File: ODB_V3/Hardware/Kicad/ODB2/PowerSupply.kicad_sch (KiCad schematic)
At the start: 53 parts, among them U13 L6981N33DR, U7 MPQ9843GLE-5-AEC1-Z

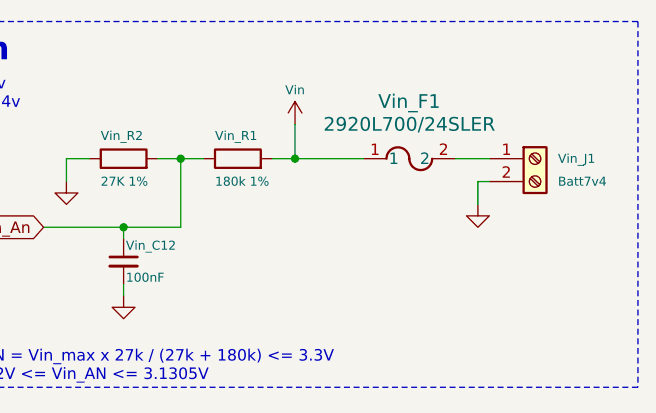
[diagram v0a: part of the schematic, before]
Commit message: fix: symbole errors and link missing footprints
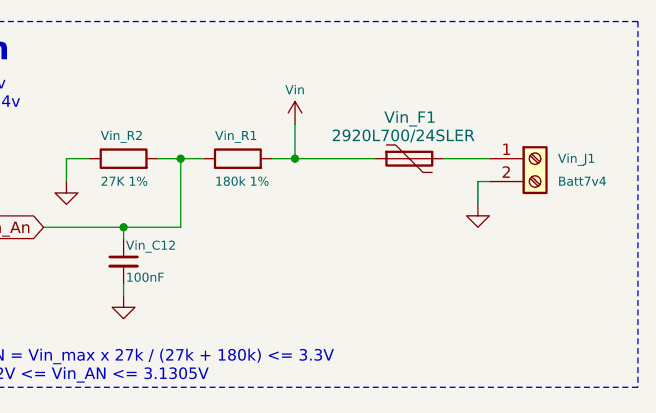
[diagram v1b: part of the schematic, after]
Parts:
- removed Vin_F1: 2920L700/24SLER, Fuse:Fuse_2920_7451Metric, symbol RGEF1400:RGEF1400
- added Vin_F1: 2920L700/24SLER, Fuse:Fuse_2920_7451Metric, symbol Device:Polyfuse
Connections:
- net Vin: now also Vin_F1.1
- net at Vin_J1.1 (Pin_1): now also Vin_F1.2
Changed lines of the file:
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@@
 	(wire
 		(pts
+			(xy 261.62 27.94) (xy 266.7 27.94)
+		)
+		(stroke
+			(width 0)
+			(type default)
+		)
+	)
+	(wire
+		(pts
 			(xy 68.58 35.56) (xy 68.58 34.29)
 		)
@@
 	(wire
 		(pts
-			(xy 245.11 27.94) (xy 252.73 27.94)
+			(xy 245.11 27.94) (xy 254 27.94)
 		)
 		(stroke
@@
 	(wire
 		(pts
-			(xy 262.89 27.94) (xy 266.7 27.94)
-		)
-		(stroke
-			(width 0)
-			(type default)
-		)
-	)
-	(wire
-		(pts
 			(xy 30.48 113.03) (xy 30.48 114.3)
 		)
@@
 	)
 	(symbol
-		(lib_id "RGEF1400:RGEF1400")
-		(at 252.73 27.94 0)
-		(unit 1)
-		(exclude_from_sim no)
-		(in_bom yes)
-		(on_board yes)
-		(dnp no)
-		(fields_autoplaced yes)
-		(property "Reference" "Vin_F1"
-			(at 257.81 21.59 0)
-			(effects
-				(font
-					(size 1.524 1.524)
-				)
-			)
-		)
-		(property "Value" "2920L700/24SLER"
-			(at 257.81 24.13 0)
-			(effects
-				(font
-					(size 1.524 1.524)
-				)
-			)
-		)
-		(property "Footprint" "Fuse:Fuse_2920_7451Metric"
-			(at 252.73 27.94 0)
-			(effects
-				(font
-					(size 1.27 1.27)
-					(italic yes)
-				)
-				(hide yes)
-			)
-		)
-		(property "Datasheet" "2920L700/12MR"
-			(at 252.73 27.94 0)
-			(effects
-				(font
-					(size 1.27 1.27)
-					(italic yes)
-				)
-				(hide yes)
-			)
-		)
-		(property "Description" ""
-			(at 252.73 27.94 0)
-			(effects
-				(font
-					(size 1.27 1.27)
-				)
-				(hide yes)
-			)
-		)
-		(pin "1"
-		)
-		(pin "2"
-		)
-		(instances
-			(project "ODB2"
-				(path "/4b06c5d1-aa8b-48ed-8972-b43a60cfab78/a0dfa29e-ccca-4096-8481-c7e33c67aac5"
-					(reference "Vin_F1")
-					(unit 1)
-				)
-			)
-		)
-	)
-	(symbol
 		(lib_id "power:GND")
 		(at 87.63 158.75 0)
@@
 					(unit 1)
 				)
+			)
+		)
+	)
+	(symbol
+		(lib_id "Device:Polyfuse")
+		(at 257.81 27.94 90)
+		(mirror x)
+		(unit 1)
+		(exclude_from_sim no)
+		(in_bom yes)
+		(on_board yes)
+		(dnp no)
+		(property "Reference" "Vin_F1"
+			(at 255.016 23.368 90)
+			(effects
+				(font
+					(size 1.27 1.27)
+				)
+				(justify right)
+			)
+		)
+		(property "Value" "2920L700/24SLER"
+			(at 249.174 25.4 90)
+			(effects
+				(font
+					(size 1.27 1.27)
+				)
+				(justify right)
+			)
+		)
+		(property "Footprint" "Fuse:Fuse_2920_7451Metric"
+			(at 262.89 29.21 0)
+			(effects
+				(font
+					(size 1.27 1.27)
+				)
+				(justify left)
+				(hide yes)
+			)
+		)
+		(property "Datasheet" "2920L700/24SLER"
+			(at 257.81 27.94 0)
+			(effects
+				(font
+					(size 1.27 1.27)
+				)
+				(hide yes)
+			)
+		)
+		(property "Description" "Resettable fuse"
+			(at 257.81 27.94 0)
+			(effects
+				(font
+					(size 1.27 1.27)
+				)
+				(hide yes)
+			)
+		)
+		(pin "2"
+		)
+		(pin "1"
+		)
+		(instances
+			(project ""
+				(path "/4b06c5d1-aa8b-48ed-8972-b43a60cfab78/a0dfa29e-ccca-4096-8481-c7e33c67aac5"
+					(reference "Vin_F1")
+					(unit 1)
+				)

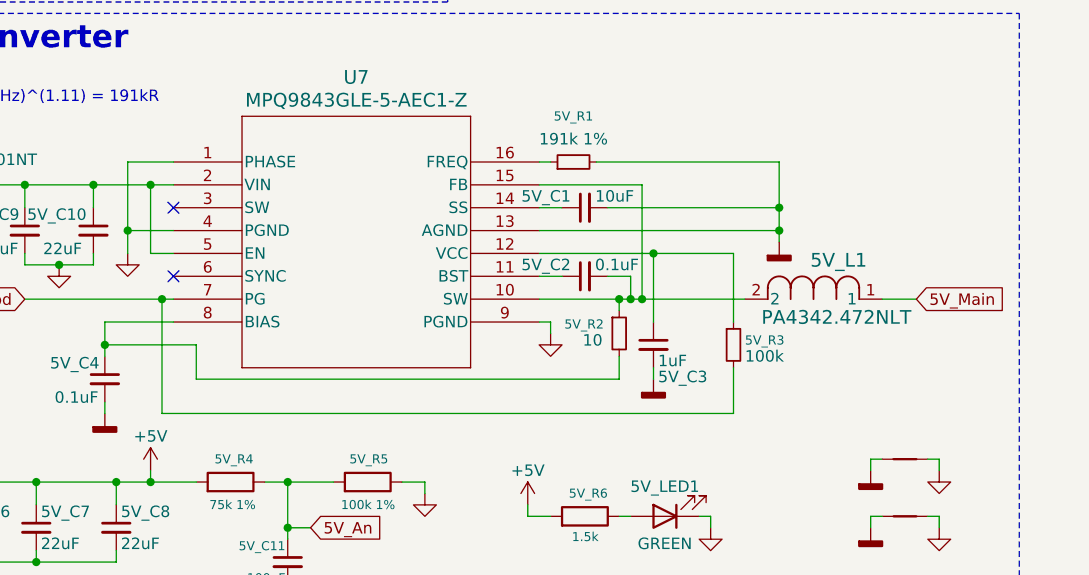
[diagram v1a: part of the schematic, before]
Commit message: fix: bias + FB feedback after inductance in buck converter 5V
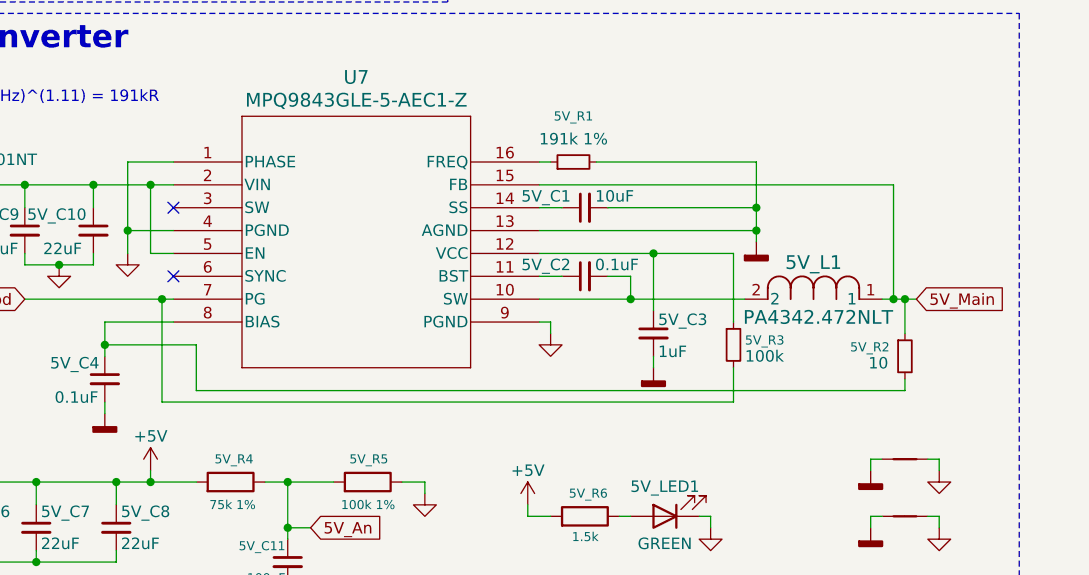
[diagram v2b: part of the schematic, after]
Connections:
- net +5V: now also 5V_R2.1, U7.15 (FB)
- net at 5V_C2.2, 5V_L1.2, U7.10 (SW): no longer 5V_R2.1, U7.15 (FB)
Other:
- moved on the sheet: 5V_C3, 5V_R2
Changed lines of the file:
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@@
 	)
 	(junction
-		(at 130.81 73.66)
+		(at 128.27 73.66)
 		(diameter 0)
 		(color 0 0 0 0)
@@
 	)
 	(junction
+		(at 143.51 83.82)
+		(diameter 0)
+		(color 0 0 0 0)
+	)
+	(junction
 		(at 46.99 71.12)
 		(diameter 0)
@@
 	)
 	(junction
-		(at 130.81 76.2)
+		(at 128.27 76.2)
 		(diameter 0)
 		(color 0 0 0 0)
@@
 	)
 	(junction
-		(at 115.57 83.82)
-		(diameter 0)
-		(color 0 0 0 0)
-	)
-	(junction
 		(at 83.82 181.61)
 		(diameter 0)
@@
 	)
 	(junction
-		(at 113.03 83.82)
-		(diameter 0)
-		(color 0 0 0 0)
-	)
-	(junction
 		(at 63.5 41.91)
 		(diameter 0)
@@
 		(color 0 0 0 0)
 	)
+	(junction
+		(at 144.78 83.82)
+		(diameter 0)
+		(color 0 0 0 0)
+	)
 	(no_connect
 		(at 63.5 73.66)
@@
 	(wire
 		(pts
-			(xy 110.49 68.58) (xy 130.81 68.58)
+			(xy 110.49 68.58) (xy 128.27 68.58)
+		)
+		(stroke
+			(width 0)
+			(type default)
+		)
+	)
+	(wire
+		(pts
+			(xy 143.51 83.82) (xy 144.78 83.82)
 		)
 		(stroke
@@
 	(wire
 		(pts
-			(xy 130.81 68.58) (xy 130.81 73.66)
+			(xy 144.78 83.82) (xy 144.78 87.63)
 		)
 		(stroke
@@
 	(wire
 		(pts
-			(xy 62.23 96.52) (xy 62.23 83.82)
+			(xy 128.27 68.58) (xy 128.27 73.66)
+		)
+		(stroke
+			(width 0)
+			(type default)
+		)
+	)
+	(wire
+		(pts
+			(xy 62.23 95.25) (xy 62.23 83.82)
 		)
 		(stroke
@@
 	(wire
 		(pts
-			(xy 66.04 92.71) (xy 66.04 88.9)
+			(xy 66.04 93.98) (xy 66.04 88.9)
 		)
 		(stroke
@@
 	(wire
 		(pts
-			(xy 142.24 83.82) (xy 146.05 83.82)
+			(xy 142.24 83.82) (xy 143.51 83.82)
 		)
 		(stroke
@@
 	(wire
 		(pts
-			(xy 113.03 90.17) (xy 113.03 92.71)
-		)
-		(stroke
-			(width 0)
-			(type default)
-		)
-	)
-	(wire
-		(pts
 			(xy 57.15 185.42) (xy 48.26 185.42)
 		)
@@
 	(wire
 		(pts
-			(xy 130.81 73.66) (xy 130.81 76.2)
+			(xy 128.27 73.66) (xy 128.27 76.2)
 		)
 		(stroke
@@
 	(wire
 		(pts
-			(xy 113.03 83.82) (xy 114.3 83.82)
-		)
-		(stroke
-			(width 0)
-			(type default)
-		)
-	)
-	(wire
-		(pts
 			(xy 91.44 105.41) (xy 91.44 104.14)
 		)
@@
 	(wire
 		(pts
-			(xy 104.14 83.82) (xy 113.03 83.82)
+			(xy 104.14 83.82) (xy 114.3 83.82)
 		)
 		(stroke
@@
 	(wire
 		(pts
-			(xy 113.03 83.82) (xy 113.03 85.09)
-		)
-		(stroke
-			(width 0)
-			(type default)
-		)
-	)
-	(wire
-		(pts
 			(xy 30.48 41.91) (xy 39.37 41.91)
 		)
@@
 	(wire
 		(pts
-			(xy 116.84 91.44) (xy 116.84 92.71)
+			(xy 48.26 113.03) (xy 39.37 113.03)
 		)
 		(stroke
@@
 	(wire
 		(pts
-			(xy 48.26 113.03) (xy 39.37 113.03)
+			(xy 144.78 83.82) (xy 146.05 83.82)
 		)
 		(stroke
@@
 	(wire
 		(pts
-			(xy 62.23 96.52) (xy 125.73 96.52)
+			(xy 62.23 95.25) (xy 125.73 95.25)
 		)
 		(stroke
@@
 	(wire
 		(pts
-			(xy 114.3 83.82) (xy 115.57 83.82)
+			(xy 114.3 83.82) (xy 127 83.82)
 		)
 		(stroke
@@
 	(wire
 		(pts
-			(xy 130.81 77.47) (xy 130.81 76.2)
+			(xy 128.27 77.47) (xy 128.27 76.2)
 		)
 		(stroke
@@
 	(wire
 		(pts
-			(xy 104.14 76.2) (xy 130.81 76.2)
+			(xy 104.14 76.2) (xy 128.27 76.2)
 		)
 		(stroke
@@
 	(wire
 		(pts
-			(xy 113.03 92.71) (xy 66.04 92.71)
+			(xy 66.04 93.98) (xy 144.78 93.98)
 		)
 		(stroke
@@
 	(wire
 		(pts
-			(xy 116.84 86.36) (xy 116.84 78.74)
+			(xy 116.84 85.09) (xy 116.84 78.74)
 		)
 		(stroke
@@
 	(wire
 		(pts
-			(xy 115.57 83.82) (xy 127 83.82)
+			(xy 116.84 91.44) (xy 116.84 90.17)
 		)
 		(stroke
@@
 	(wire
 		(pts
-			(xy 104.14 71.12) (xy 115.57 71.12)
+			(xy 104.14 71.12) (xy 143.51 71.12)
 		)
 		(stroke
@@
 	(wire
 		(pts
-			(xy 125.73 91.44) (xy 125.73 96.52)
+			(xy 125.73 91.44) (xy 125.73 95.25)
 		)
 		(stroke
@@
 	(wire
 		(pts
-			(xy 111.76 73.66) (xy 130.81 73.66)
+			(xy 111.76 73.66) (xy 128.27 73.66)
 		)
 		(stroke
@@
 	(wire
 		(pts
-			(xy 115.57 71.12) (xy 115.57 83.82)
+			(xy 143.51 71.12) (xy 143.51 83.82)
 		)
 		(stroke
@@
 	(wire
 		(pts
+			(xy 144.78 93.98) (xy 144.78 92.71)
+		)
+		(stroke
+			(width 0)
+			(type default)
+		)
+	)
+	(wire
+		(pts
 			(xy 217.17 35.56) (xy 226.06 35.56)
 		)
@@
 	(symbol
 		(lib_id "power:GNDD")
-		(at 130.81 77.47 0)
+		(at 128.27 77.47 0)
 		(unit 1)
 		(exclude_from_sim no)
@@
 		(fields_autoplaced yes)
 		(property "Reference" "#PWR06"
-			(at 130.81 83.82 0)
+			(at 128.27 83.82 0)
 			(effects
 				(font
@@
 		)
 		(property "Value" "AGND5V"
-			(at 130.81 81.28 0)
+			(at 128.27 81.28 0)
 			(effects
 				(font
@@
 		)
 		(property "Footprint" ""
-			(at 130.81 77.47 0)
+			(at 128.27 77.47 0)
 			(effects
 				(font
@@
 		)
 		(property "Datasheet" ""
-			(at 130.81 77.47 0)
+			(at 128.27 77.47 0)
 			(effects
 				(font
@@
 		)
 		(property "Description" "Power symbol creates a global label with name \"GNDD\" , digital ground"
-			(at 130.81 77.47 0)
+			(at 128.27 77.47 0)
 			(effects
 				(font
@@
 		(dnp no)
 		(property "Reference" "5V_L1"
-			(at 137.414 79.502 0)
+			(at 134.62 79.756 0)
 			(effects
 				(font
@@
 		)
 		(property "Value" "PA4342.472NLT"
-			(at 137.16 85.852 0)
+			(at 135.128 85.852 0)
 			(effects
 				(font
@@
 	(symbol
 		(lib_id "power:GNDD")
-		(at 116.84 92.71 0)
+		(at 116.84 91.44 0)
 		(unit 1)
 		(exclude_from_sim no)
@@
 		(fields_autoplaced yes)
 		(property "Reference" "#PWR02"
-			(at 116.84 99.06 0)
+			(at 116.84 97.79 0)
 			(effects
 				(font
@@
 		)
 		(property "Value" "AGND5V"
-			(at 116.84 96.52 0)
+			(at 116.84 95.25 0)
 			(effects
 				(font
@@
 		)
 		(property "Footprint" ""
-			(at 116.84 92.71 0)
+			(at 116.84 91.44 0)
 			(effects
 				(font
@@
 		)
 		(property "Datasheet" ""
-			(at 116.84 92.71 0)
+			(at 116.84 91.44 0)
 			(effects
 				(font
@@
 		)
 		(property "Description" "Power symbol creates a global label with name \"GNDD\" , digital ground"
-			(at 116.84 92.71 0)
+			(at 116.84 91.44 0)
 			(effects
 				(font
@@
 	(symbol
 		(lib_id "Device:R_Small")
-		(at 113.03 87.63 0)
+		(at 144.78 90.17 0)
 		(unit 1)
 		(exclude_from_sim no)
@@
 		(dnp no)
 		(property "Reference" "5V_R2"
-			(at 106.934 86.614 0)
+			(at 138.684 89.154 0)
 			(effects
 				(font
@@
 		)
 		(property "Value" "10"
-			(at 108.966 88.392 0)
+			(at 140.716 90.932 0)
 			(effects
 				(font
@@
 		)
 		(property "Footprint" "Resistor_SMD:R_0603_1608Metric"
-			(at 113.03 87.63 0)
+			(at 144.78 90.17 0)
 			(effects
 				(font
@@
 		)
 		(property "Datasheet" "~"
-			(at 113.03 87.63 0)
+			(at 144.78 90.17 0)
 			(effects
 				(font
@@
 		)
 		(property "Description" "Resistor, small symbol"
-			(at 113.03 87.63 0)
+			(at 144.78 90.17 0)
 			(effects
 				(font
@@
 		)
 		(instances
-			(project ""
+			(project "ODB2"
 				(path "/4b06c5d1-aa8b-48ed-8972-b43a60cfab78/a0dfa29e-ccca-4096-8481-c7e33c67aac5"
 					(reference "5V_R2")
@@
 	(symbol
 		(lib_id "Device:C_Small")
-		(at 116.84 88.9 0)
+		(at 116.84 87.63 0)
 		(unit 1)
 		(exclude_from_sim no)
@@
 		(dnp no)
 		(property "Reference" "5V_C3"
-			(at 117.348 92.456 0)
+			(at 117.348 86.106 0)
 			(effects
 				(font
@@
 		)
 		(property "Value" "1uF"
-			(at 117.348 90.678 0)
+			(at 117.348 89.662 0)
 			(effects
 				(font
@@
 		)
 		(property "Footprint" "Capacitor_SMD:C_0603_1608Metric"
-			(at 116.84 88.9 0)
+			(at 116.84 87.63 0)
 			(effects
 				(font
@@
 		)
 		(property "Datasheet" "~"
-			(at 116.84 88.9 0)
+			(at 116.84 87.63 0)
 			(effects
 				(font
@@
 		)
 		(property "Description" "Unpolarized capacitor, small symbol"
-			(at 116.84 88.9 0)
+			(at 116.84 87.63 0)
 			(effects
 				(font

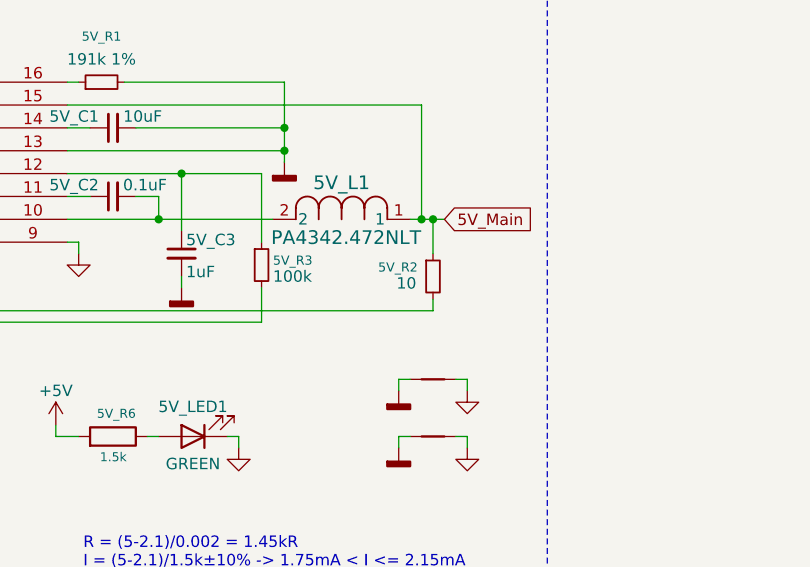
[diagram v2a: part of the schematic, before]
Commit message: fix label 5V_R2
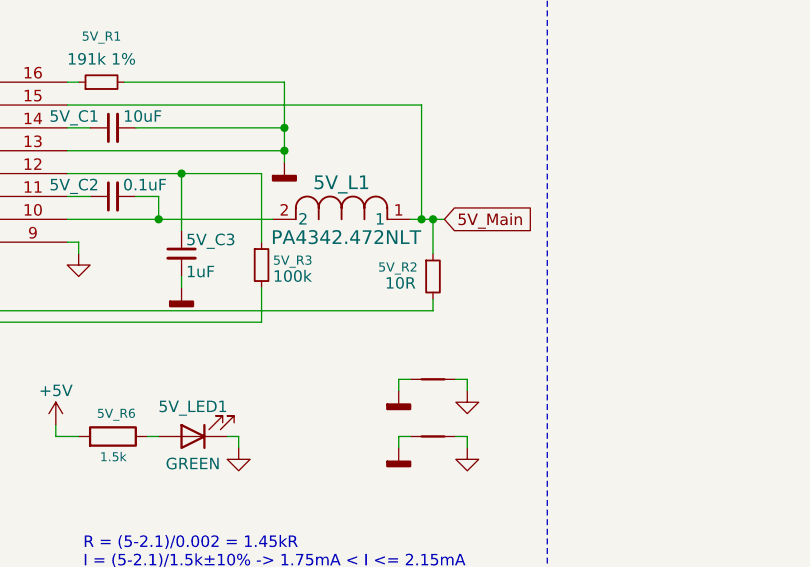
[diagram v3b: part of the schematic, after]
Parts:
- 5V_R2: value 10 -> 10R
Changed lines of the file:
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@@
 			)
 		)
-		(property "Value" "10"
-			(at 140.716 90.932 0)
+		(property "Value" "10R"
+			(at 139.446 90.932 0)
 			(effects
 				(font

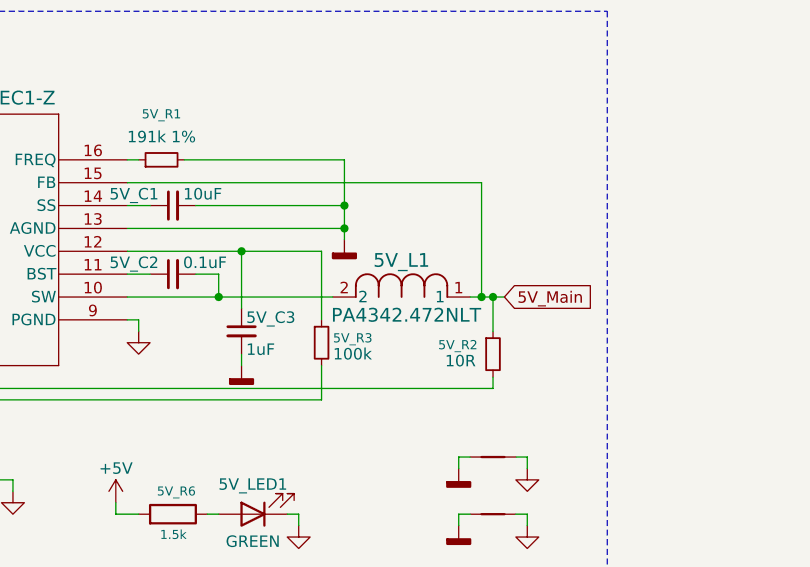
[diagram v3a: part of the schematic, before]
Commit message: fix: some footprints/symboles link + add criticalLed pin
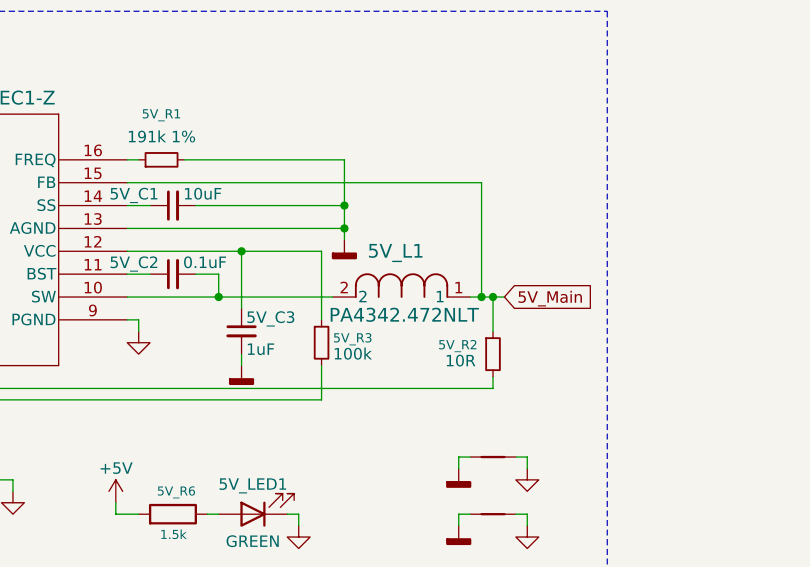
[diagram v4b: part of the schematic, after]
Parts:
- 5V_L1: footprint IND_PA4342_PUL -> ODB:IND_PA4342_PUL
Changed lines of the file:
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@@
+	)
+	(symbol
+		(lib_name "PA4342.472NLT_1")
+		(lib_id "ODB2:PA4342.472NLT")
+		(at 127 83.82 0)
+		(unit 1)
+		(exclude_from_sim no)
+		(in_bom yes)
+		(on_board yes)
+		(dnp no)
+		(property "Reference" "5V_L1"
+			(at 133.985 78.74 0)
+			(effects
+				(font
+					(size 1.524 1.524)
+				)
+			)
+		)
+		(property "Value" "PA4342.472NLT"
+			(at 134.874 85.852 0)
+			(effects
+				(font
+					(size 1.524 1.524)
+				)
+			)
+		)
+		(property "Footprint" "ODB:IND_PA4342_PUL"
+			(at 127 83.82 0)
+			(effects
+				(font
+					(size 1.27 1.27)
+					(italic yes)
+				)
+				(hide yes)
+			)
+		)
+		(property "Datasheet" "PA4342.472NLT"
+			(at 127 83.82 0)
+			(effects
+				(font
+					(size 1.27 1.27)
+					(italic yes)
+				)
+				(hide yes)
+			)
+		)
+		(property "Description" ""
+			(at 127 83.82 0)
+			(effects
+				(font
+					(size 1.27 1.27)
+				)
+				(hide yes)
+			)
+		)
+		(pin "2"
+		)
+		(pin "1"
+		)
+		(instances
+			(project ""
+				(path "/4b06c5d1-aa8b-48ed-8972-b43a60cfab78/a0dfa29e-ccca-4096-8481-c7e33c67aac5"
+					(reference "5V_L1")
+					(unit 1)
+				)
+			)
+		)
 	)
 	(symbol
@@
 					(unit 1)
 				)
-			)
-		)
-	)
-	(symbol
-		(lib_id "ODB2:PA4342.472NLT")
-		(at 127 83.82 0)
-		(unit 1)
-		(exclude_from_sim no)
-		(in_bom yes)
-		(on_board yes)
-		(dnp no)
-		(property "Reference" "5V_L1"
-			(at 134.62 79.756 0)
-			(effects
-				(font
-					(size 1.524 1.524)
-				)
-			)
-		)
-		(property "Value" "PA4342.472NLT"
-			(at 135.128 85.852 0)
-			(effects
-				(font
-					(size 1.524 1.524)
-				)
-			)
-		)
-		(property "Footprint" "IND_PA4342_PUL"
-			(at 127 83.82 0)
-			(effects
-				(font
-					(size 1.27 1.27)
-					(italic yes)
-				)
-				(hide yes)
-			)
-		)
-		(property "Datasheet" "PA4342.472NLT"
-			(at 127 83.82 0)
-			(effects
-				(font
-					(size 1.27 1.27)
-					(italic yes)
-				)
-				(hide yes)
-			)
-		)
-		(property "Description" ""
-			(at 127 83.82 0)
-			(effects
-				(font
-					(size 1.27 1.27)
-				)
-				(hide yes)
-			)
-		)
-		(pin "2"
-		)
-		(pin "1"
-		)
-		(instances
-			(project ""
-				(path "/4b06c5d1-aa8b-48ed-8972-b43a60cfab78/a0dfa29e-ccca-4096-8481-c7e33c67aac5"
-					(reference "5V_L1")
-					(unit 1)
-				)
